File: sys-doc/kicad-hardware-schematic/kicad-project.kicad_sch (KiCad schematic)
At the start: 7 parts, among them J1 DHT11 (Temp/Hum), SW1 Switch (CollectTraining), SW2 Switch (IsOutlier), U1 ESP32-DevKitC

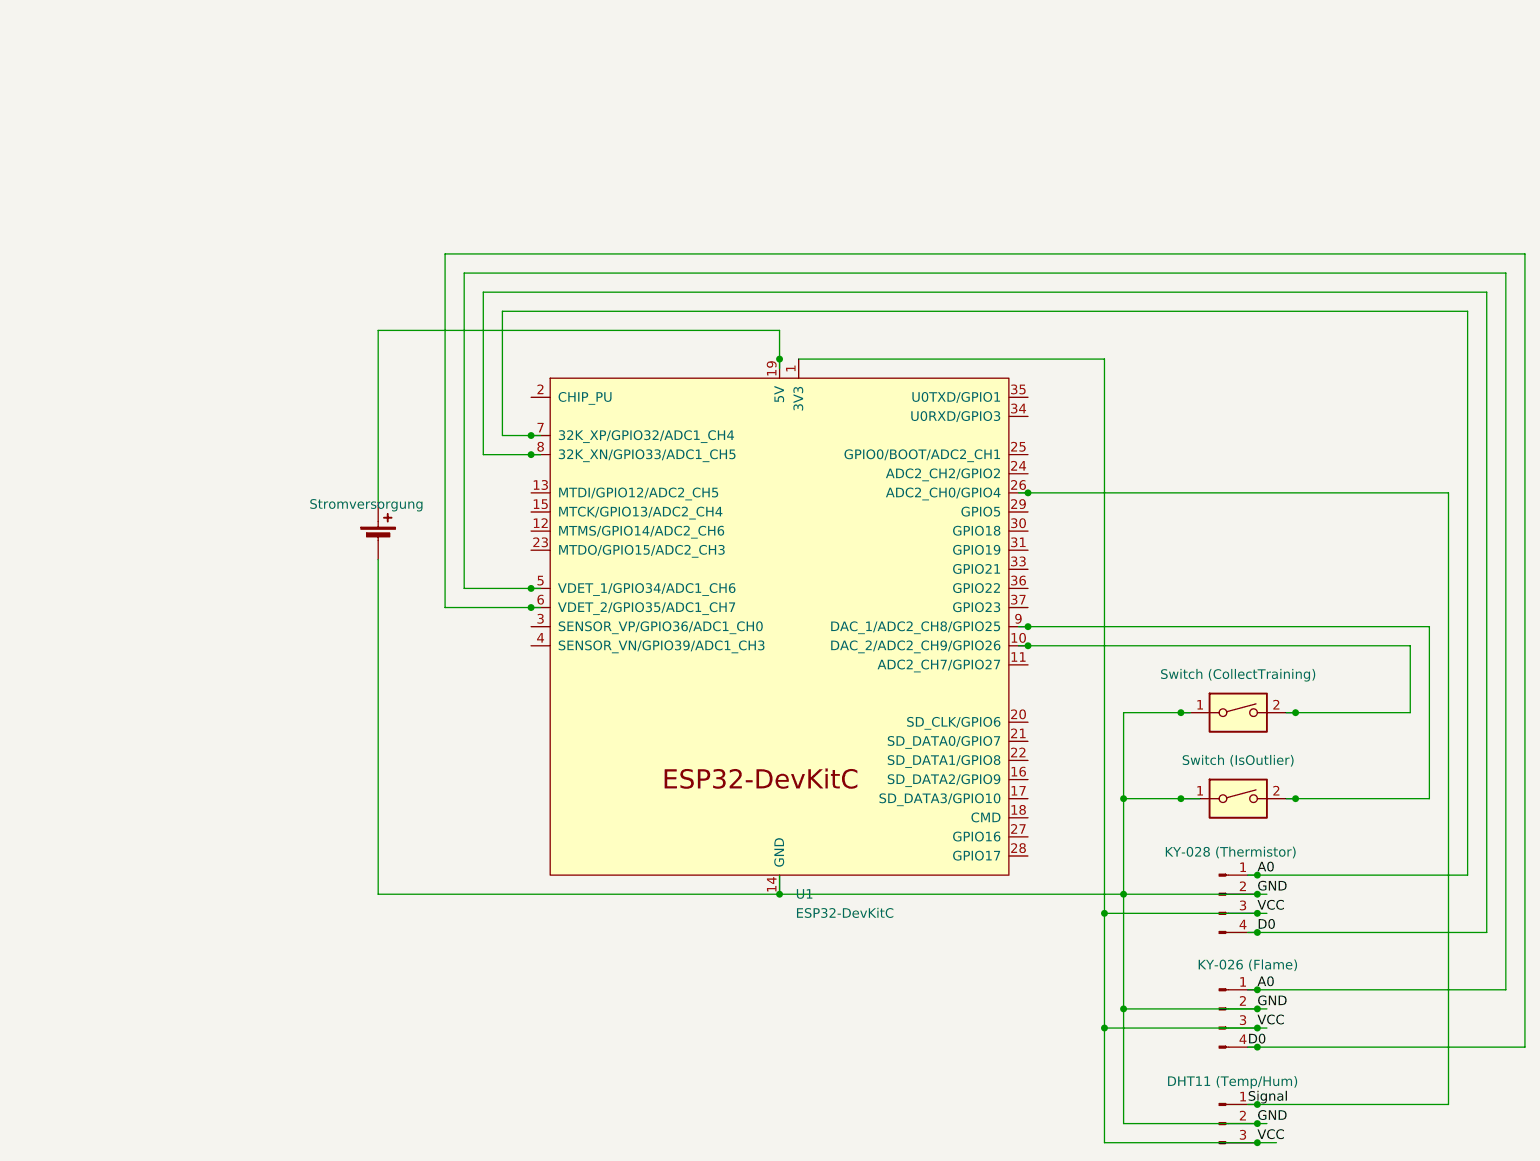
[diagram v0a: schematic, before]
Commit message: Prepare and do pdf export of KiCAD project
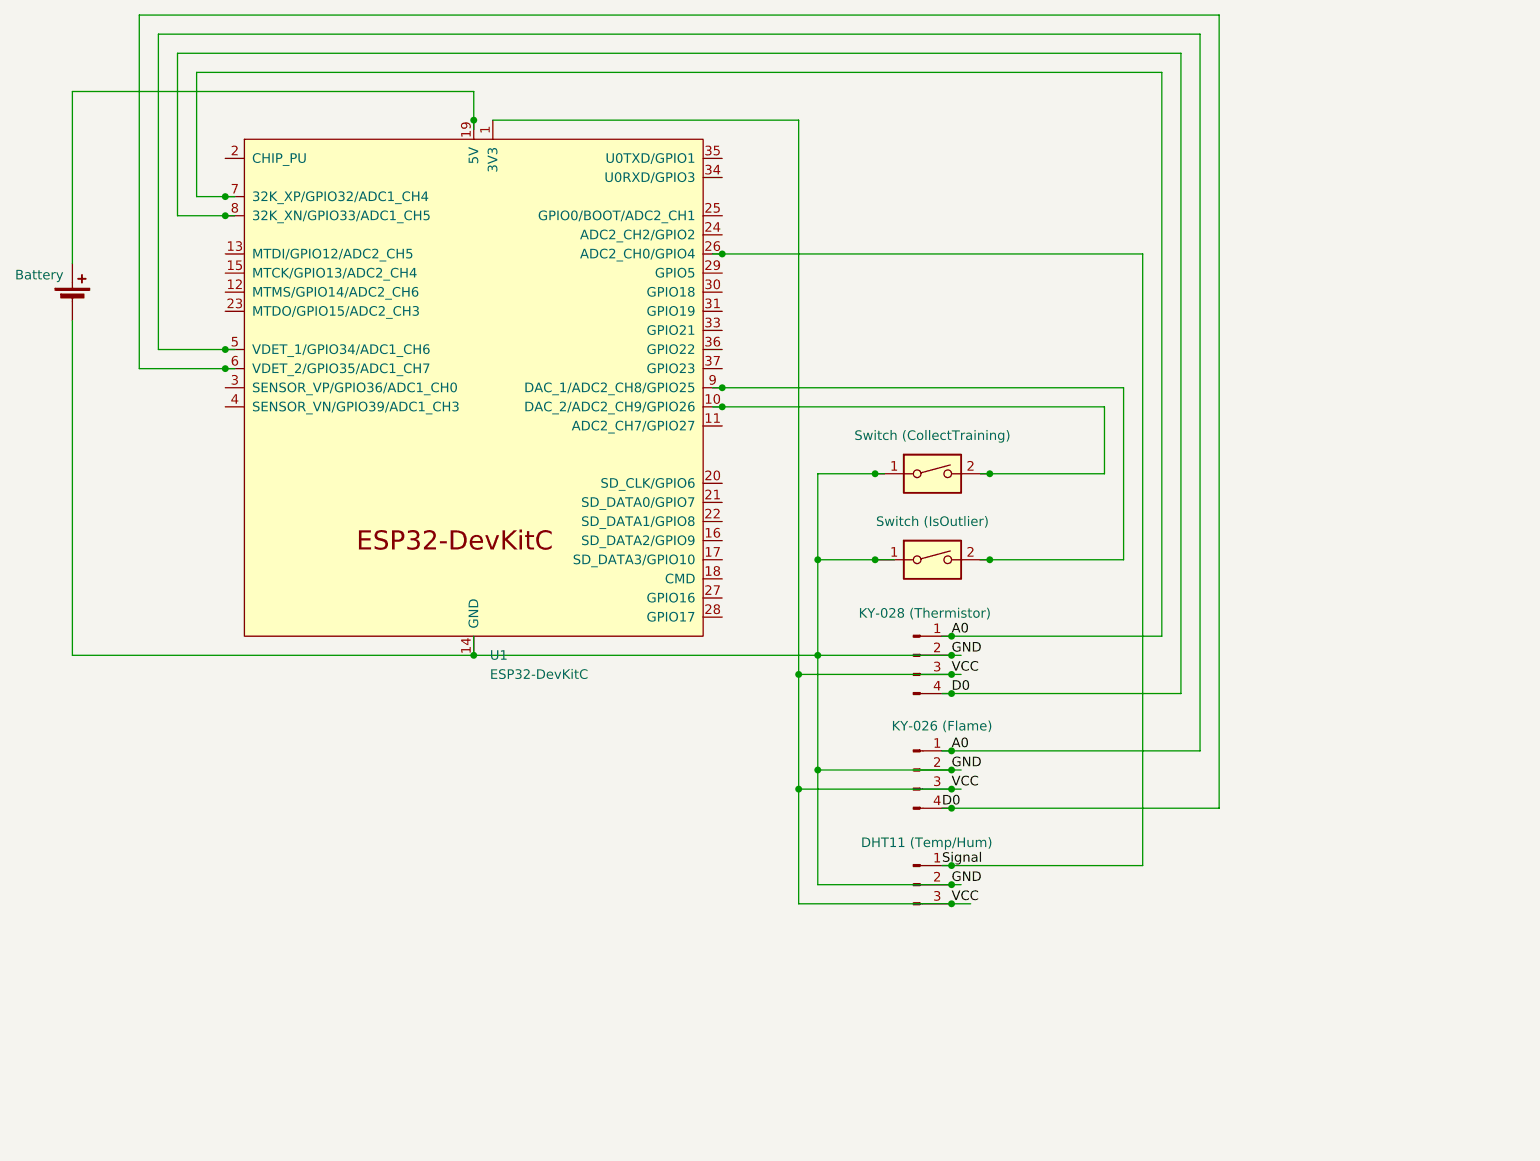
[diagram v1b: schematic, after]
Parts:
- BT1: value Stromversorgung -> Battery
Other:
- moved on the sheet: U1

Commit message: Update KiCAD project for added sensor display, export PDF
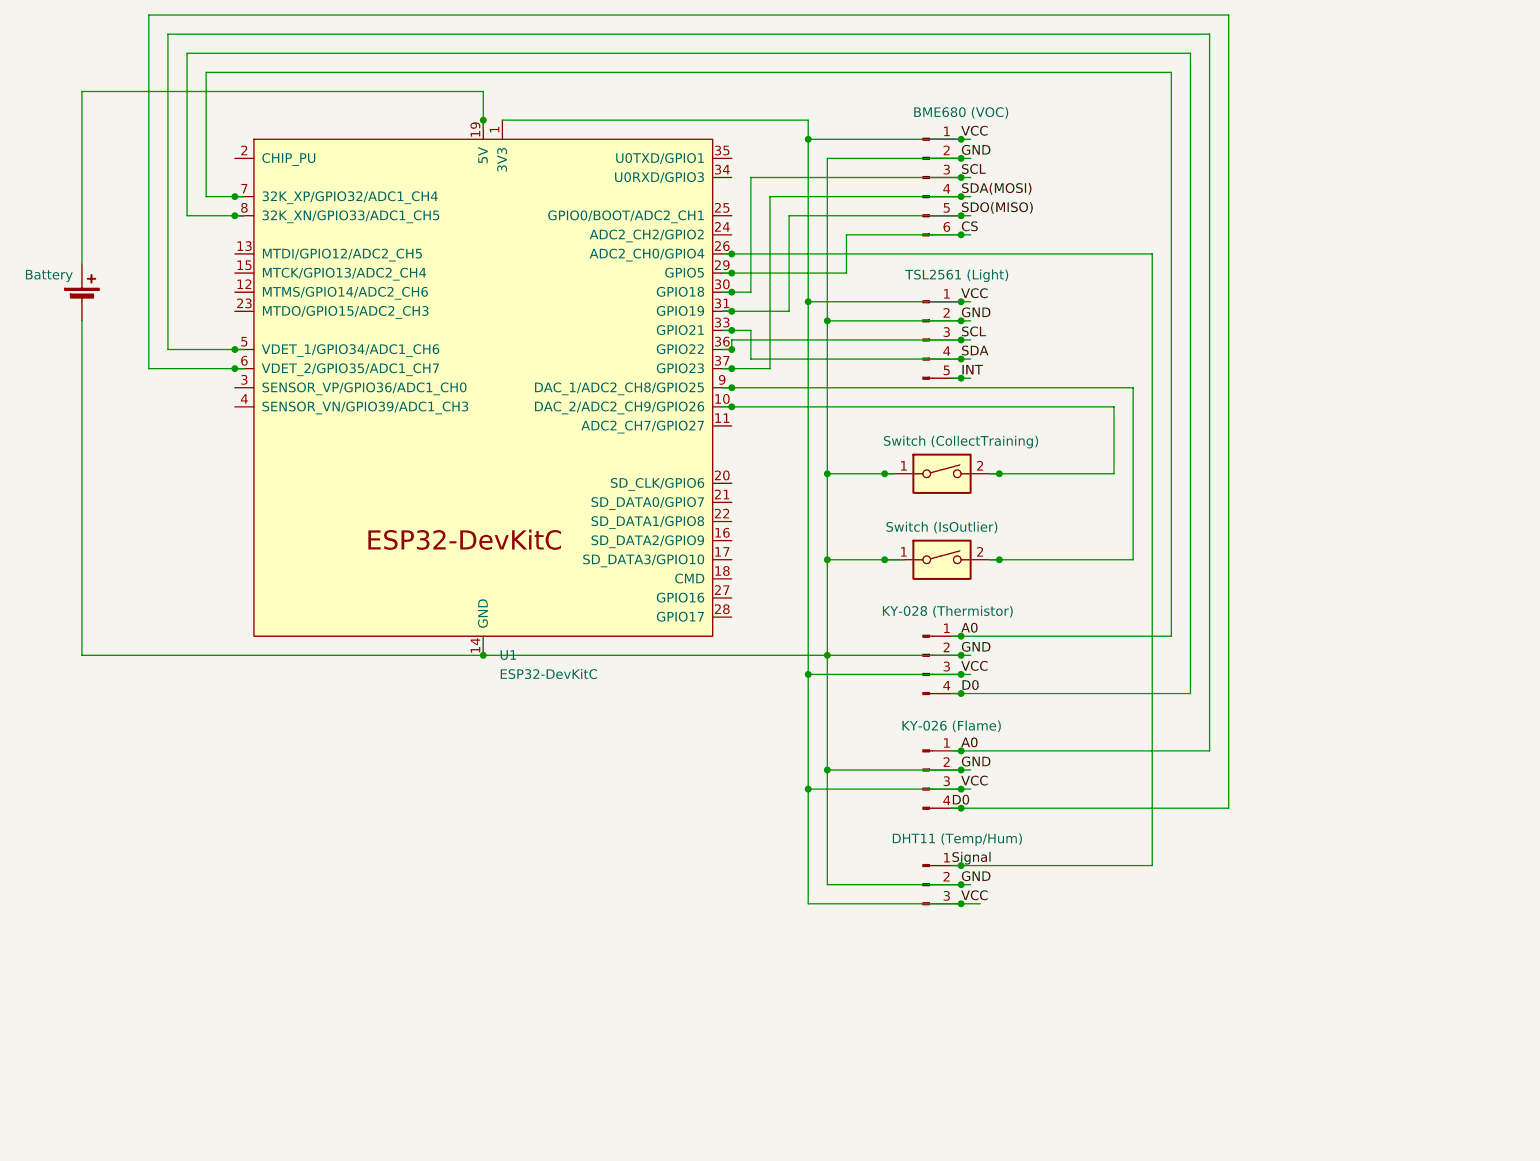
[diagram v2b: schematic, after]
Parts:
- added J2: TSL2561 (Light), symbol Connector:Conn_01x05_Pin
- added J3: BME680 (VOC), symbol Connector:Conn_01x06_Pin
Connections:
- net GND: now also J2.2 (Pin_2), J3.2 (Pin_2)
- net VCC: now also J2.1 (Pin_1), J3.1 (Pin_1)
- net CS: now reaches U1.29 (GPIO5)
- net CS: now also J3.6 (Pin_6)
- net SCL: now reaches U1.30 (GPIO18)
- net SCL: now also U1.36 (GPIO22), J2.3 (Pin_3), J3.3 (Pin_3)
- net SDO(MISO): now reaches U1.31 (GPIO19)
- net SDO(MISO): now also J3.5 (Pin_5)
- net SDA: now reaches U1.33 (GPIO21)
- net SDA: now also J2.4 (Pin_4)
- net SDA(MOSI): now reaches U1.37 (GPIO23)
- net SDA(MOSI): now also J3.4 (Pin_4)
- new net INT: J2.5 (Pin_5)
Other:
- moved on the sheet: U1
